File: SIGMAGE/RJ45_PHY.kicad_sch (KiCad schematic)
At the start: 18 parts, among them J6 18407728, U9 LAN8720ACP, X2 STDCSK425M

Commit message: Finished schematic
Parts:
- added R31: 10k, symbol Device:R
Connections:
- net +3V3: now also R31.2
- net PHY_NRST: now reaches U9.15 (NRST)
- net PHY_NRST: now also R31.1
- net PHY_REFCLKO renamed PHY_REFCLK
- no-connect marks 4 -> 5
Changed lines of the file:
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@@
 	)
 	(junction
+		(at 240.03 86.36)
+		(diameter 0)
+		(color 0 0 0 0)
+	)
+	(junction
 		(at 86.36 50.8)
 		(diameter 0)
@@
 	)
 	(no_connect
+		(at 212.09 88.9)
+	)
+	(no_connect
 		(at 81.28 93.98)
 	)
@@
 	(wire
 		(pts
+			(xy 240.03 86.36) (xy 247.65 86.36)
+		)
+		(stroke
+			(width 0)
+			(type default)
+		)
+	)
+	(wire
+		(pts
 			(xy 215.9 106.68) (xy 212.09 106.68)
 		)
@@
 	(wire
 		(pts
+			(xy 240.03 69.85) (xy 240.03 72.39)
+		)
+		(stroke
+			(width 0)
+			(type default)
+		)
+	)
+	(wire
+		(pts
 			(xy 91.44 158.75) (xy 102.87 158.75)
 		)
@@
 	(wire
 		(pts
+			(xy 240.03 80.01) (xy 240.03 86.36)
+		)
+		(stroke
+			(width 0)
+			(type default)
+		)
+	)
+	(wire
+		(pts
 			(xy 93.98 59.69) (xy 93.98 81.28)
 		)
@@
 	(wire
 		(pts
+			(xy 212.09 86.36) (xy 240.03 86.36)
+		)
+		(stroke
+			(width 0)
+			(type default)
+		)
+	)
+	(wire
+		(pts
 			(xy 234.95 124.46) (xy 234.95 129.54)
 		)
@@
 		)
 	)
+	(global_label "PHY_NRST"
+		(shape input)
+		(at 247.65 86.36 0)
+		(fields_autoplaced yes)
+		(effects
+			(font
+				(size 1.27 1.27)
+			)
+			(justify left)
+		)
+		(property "Intersheetrefs" "${INTERSHEET_REFS}"
+			(at 260.0695 86.36 0)
+			(effects
+				(font
+					(size 1.27 1.27)
+				)
+				(justify left)
+				(hide yes)
+			)
+		)
+	)
 	(global_label "PHY_MDIO"
 		(shape bidirectional)
@@
 		)
 	)
-	(global_label "PHY_REFCLKO"
+	(global_label "PHY_REFCLK"
 		(shape output)
 		(at 212.09 73.66 0)
@@
 		)
 		(property "Intersheetrefs" "${INTERSHEET_REFS}"
-			(at 228.1381 73.66 0)
+			(at 226.8076 73.66 0)
 			(effects
 				(font
@@
 	)
 	(symbol
+		(lib_id "power:+5V")
+		(at 240.03 69.85 0)
+		(unit 1)
+		(exclude_from_sim no)
+		(in_bom yes)
+		(on_board yes)
+		(dnp no)
+		(fields_autoplaced yes)
+		(property "Reference" "#PWR099"
+			(at 240.03 73.66 0)
+			(effects
+				(font
+					(size 1.27 1.27)
+				)
+				(hide yes)
+			)
+		)
+		(property "Value" "+3V3"
+			(at 240.03 64.77 0)
+			(effects
+				(font
+					(size 1.27 1.27)
+				)
+			)
+		)
+		(property "Footprint" ""
+			(at 240.03 69.85 0)
+			(effects
+				(font
+					(size 1.27 1.27)
+				)
+				(hide yes)
+			)
+		)
+		(property "Datasheet" ""
+			(at 240.03 69.85 0)
+			(effects
+				(font
+					(size 1.27 1.27)
+				)
+				(hide yes)
+			)
+		)
+		(property "Description" "Power symbol creates a global label with name \"+5V\""
+			(at 240.03 69.85 0)
+			(effects
+				(font
+					(size 1.27 1.27)
+				)
+				(hide yes)
+			)
+		)
+		(pin "1"
+		)
+		(instances
+			(project "SIGMAGE"
+				(path "/6fbe3371-b6a3-4e28-aef4-4e5865f4674e/c7230a02-11e8-4e0e-86c6-3c608fa6bb1d"
+					(reference "#PWR099")
+					(unit 1)
+				)
+			)
+		)
+	)
+	(symbol
 		(lib_id "power:GND")
 		(at 38.1 114.3 0)
@@
 		(on_board yes)
 		(dnp no)
-		(fields_autoplaced yes)
 		(property "Reference" "U9"
-			(at 186.055 58.42 0)
+			(at 169.418 61.976 0)
 			(effects
 				(font
@@
 		)
 		(property "Value" "LAN8720ACP"
-			(at 186.055 60.96 0)
+			(at 174.752 110.998 0)
 			(effects
 				(font
@@
 					(unit 1)
 				)
+			)
+		)
+	)
+	(symbol
+		(lib_id "Device:R")
+		(at 240.03 76.2 180)
+		(unit 1)
+		(exclude_from_sim no)
+		(in_bom yes)
+		(on_board yes)
+		(dnp no)
+		(property "Reference" "R31"
+			(at 241.808 74.93 0)
+			(effects
+				(font
+					(size 1.27 1.27)
+				)
+				(justify right)
+			)
+		)
+		(property "Value" "10k"
+			(at 241.808 77.47 0)
+			(effects
+				(font
+					(size 1.27 1.27)
+				)
+				(justify right)
+			)
+		)
+		(property "Footprint" ""
+			(at 241.808 76.2 90)
+			(effects
+				(font
+					(size 1.27 1.27)
+				)
+				(hide yes)
+			)
+		)
+		(property "Datasheet" "~"
+			(at 240.03 76.2 0)
+			(effects
+				(font
+					(size 1.27 1.27)
+				)
+				(hide yes)
+			)
+		)
+		(property "Description" "Resistor"
+			(at 240.03 76.2 0)
+			(effects
+				(font
+					(size 1.27 1.27)
+				)
+				(hide yes)
+			)
+		)
+		(pin "2"
+		)
+		(pin "1"
+		)
+		(instances
+			(project "SIGMAGE"
+				(path "/6fbe3371-b6a3-4e28-aef4-4e5865f4674e/c7230a02-11e8-4e0e-86c6-3c608fa6bb1d"
+					(reference "R31")
+					(unit 1)
+				)

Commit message: Added PCB layout and started routing
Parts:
- C45, C46, C47, C48, C49, C50, C51, C52: footprint (none) -> Capacitor_SMD:C_0603_1608Metric
- R24, R25, R26, R27, R28, R29, R30, R31: footprint (none) -> Resistor_SMD:R_0603_1608Metric
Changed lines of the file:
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@@
 			)
 		)
-		(property "Footprint" ""
+		(property "Footprint" "Capacitor_SMD:C_0603_1608Metric"
 			(at 147.0152 59.69 0)
 			(effects
@@
 			)
 		)
-		(property "Footprint" ""
+		(property "Footprint" "Capacitor_SMD:C_0603_1608Metric"
 			(at 235.9152 124.46 0)
 			(effects
@@
 			)
 		)
-		(property "Footprint" ""
+		(property "Footprint" "Capacitor_SMD:C_0603_1608Metric"
 			(at 157.1752 59.69 0)
 			(effects
@@
 			)
 		)
-		(property "Footprint" ""
+		(property "Footprint" "Resistor_SMD:R_0603_1608Metric"
 			(at 110.998 55.88 90)
 			(effects
@@
 			)
 		)
-		(property "Footprint" ""
+		(property "Footprint" "Capacitor_SMD:C_0603_1608Metric"
 			(at 92.4052 158.75 0)
 			(effects
@@
 			)
 		)
-		(property "Footprint" ""
+		(property "Footprint" "Resistor_SMD:R_0603_1608Metric"
 			(at 103.378 55.88 90)
 			(effects
@@
 			)
 		)
-		(property "Footprint" ""
+		(property "Footprint" "Resistor_SMD:R_0603_1608Metric"
 			(at 96.52 98.298 90)
 			(effects
@@
 			)
 		)
-		(property "Footprint" ""
+		(property "Footprint" "Capacitor_SMD:C_0603_1608Metric"
 			(at 103.8352 158.75 0)
 			(effects
@@
 			)
 		)
-		(property "Footprint" ""
+		(property "Footprint" "Resistor_SMD:R_0603_1608Metric"
 			(at 217.678 111.76 90)
 			(effects
@@
 			)
 		)
-		(property "Footprint" ""
+		(property "Footprint" "Capacitor_SMD:C_0603_1608Metric"
 			(at 256.2352 124.46 0)
 			(effects
@@
 			)
 		)
-		(property "Footprint" ""
+		(property "Footprint" "Capacitor_SMD:C_0603_1608Metric"
 			(at 115.2652 158.75 0)
 			(effects
@@
 			)
 		)
-		(property "Footprint" ""
+		(property "Footprint" "Resistor_SMD:R_0603_1608Metric"
 			(at 88.138 55.88 90)
 			(effects
@@
 			)
 		)
-		(property "Footprint" ""
+		(property "Footprint" "Resistor_SMD:R_0603_1608Metric"
 			(at 96.52 105.918 90)
 			(effects
@@
 			)
 		)
-		(property "Footprint" ""
+		(property "Footprint" "Capacitor_SMD:C_0603_1608Metric"
 			(at 80.9752 158.75 0)
 			(effects
@@
 			)
 		)
-		(property "Footprint" ""
+		(property "Footprint" "Resistor_SMD:R_0603_1608Metric"
 			(at 95.758 55.88 90)
 			(effects
@@
 			)
 		)
-		(property "Footprint" ""
+		(property "Footprint" "Resistor_SMD:R_0603_1608Metric"
 			(at 241.808 76.2 90)
 			(effects

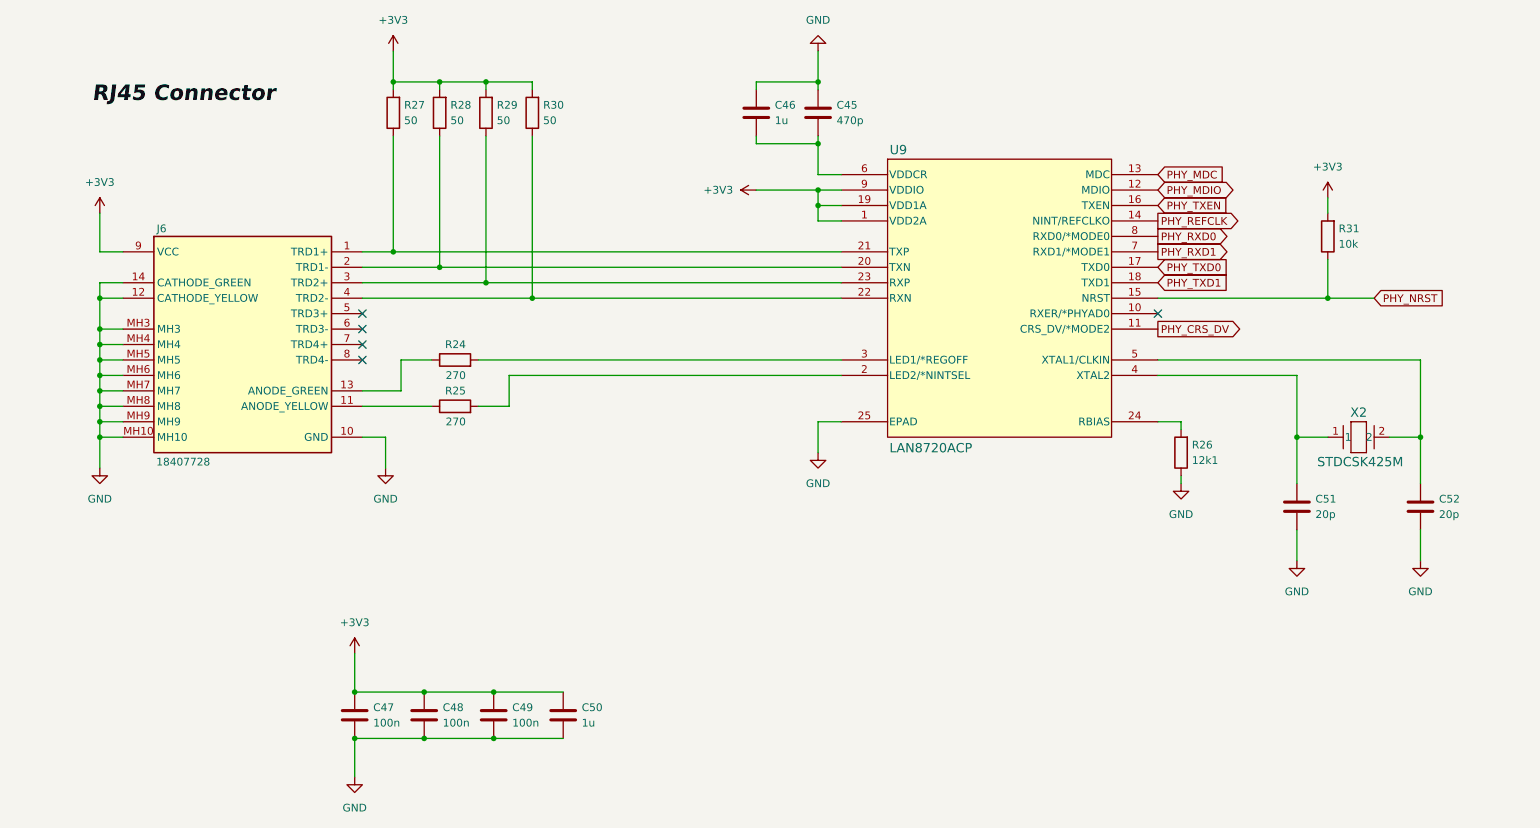
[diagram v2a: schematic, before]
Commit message: Final touches, PCB layout is still horrible, will fix in MK II
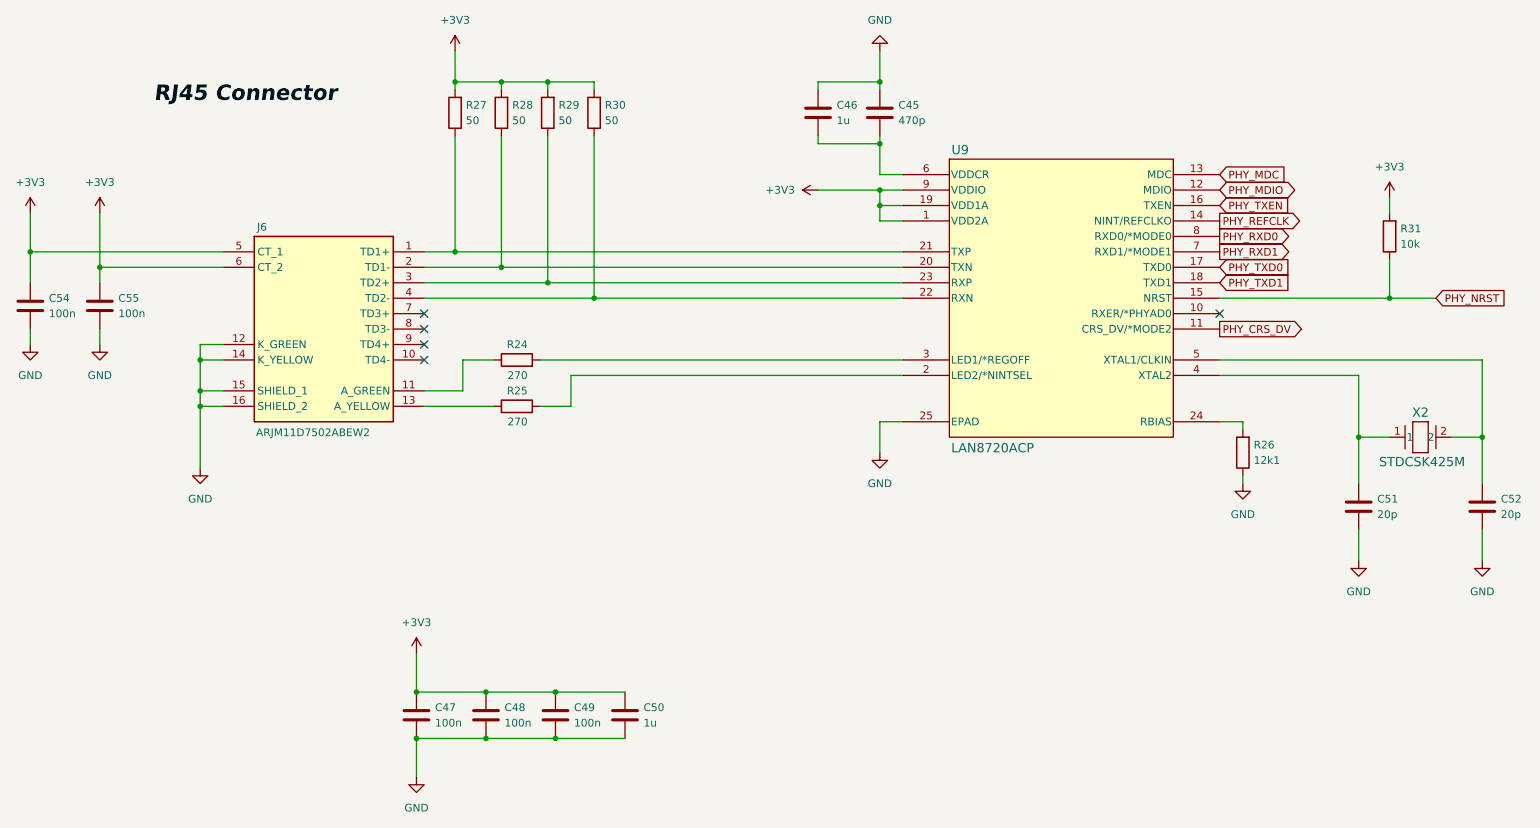
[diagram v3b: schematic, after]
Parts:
- removed J6: 18407728, SIGMAGE:18407728, symbol SIGMAGE:18407728
- added C54, C55: 100n, Capacitor_SMD:C_0603_1608Metric, symbol Device:C
- added J6: ARJM11D7502ABEW2, SIGMAGE:ARJM11D7502ABEW2, symbol SIGMAGE:ARJM11D7502ABEW2
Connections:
- net +3V3: now also C54.1, C55.1, J6.5 (CT_1), J6.6 (CT_2)
- net GND: now also C54.2, C55.2, J6.12 (K_GREEN), J6.14 (K_YELLOW), J6.15 (SHIELD_1), J6.16 (SHIELD_2)
- net at R30.1, U9.22 (RXN): now also J6.4 (TD2-)
- net at R29.1, U9.23 (RXP): now also J6.3 (TD2+)
- net at R24.1: now also J6.11 (A_GREEN)
- net at R27.1, U9.21 (TXP): now also J6.1 (TD1+)
- net at R25.1: now also J6.13 (A_YELLOW)
- net at R28.1, U9.20 (TXN): now also J6.2 (TD1-)
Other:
- moved on the sheet: C45, C46, C47, C48, C49, C50, C51, C52, R24, R25, R26, R27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
